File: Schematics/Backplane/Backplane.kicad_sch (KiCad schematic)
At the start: 21 parts, among them J1 Edge Connector (SLOT 1), J2 Edge Connector (SLOT 2), J3 Edge Connector (SLOT 3), J4 Edge Connector (SLOT 4), J5 Edge Connector (SLOT 5), J6 Conn_01x06_Socket

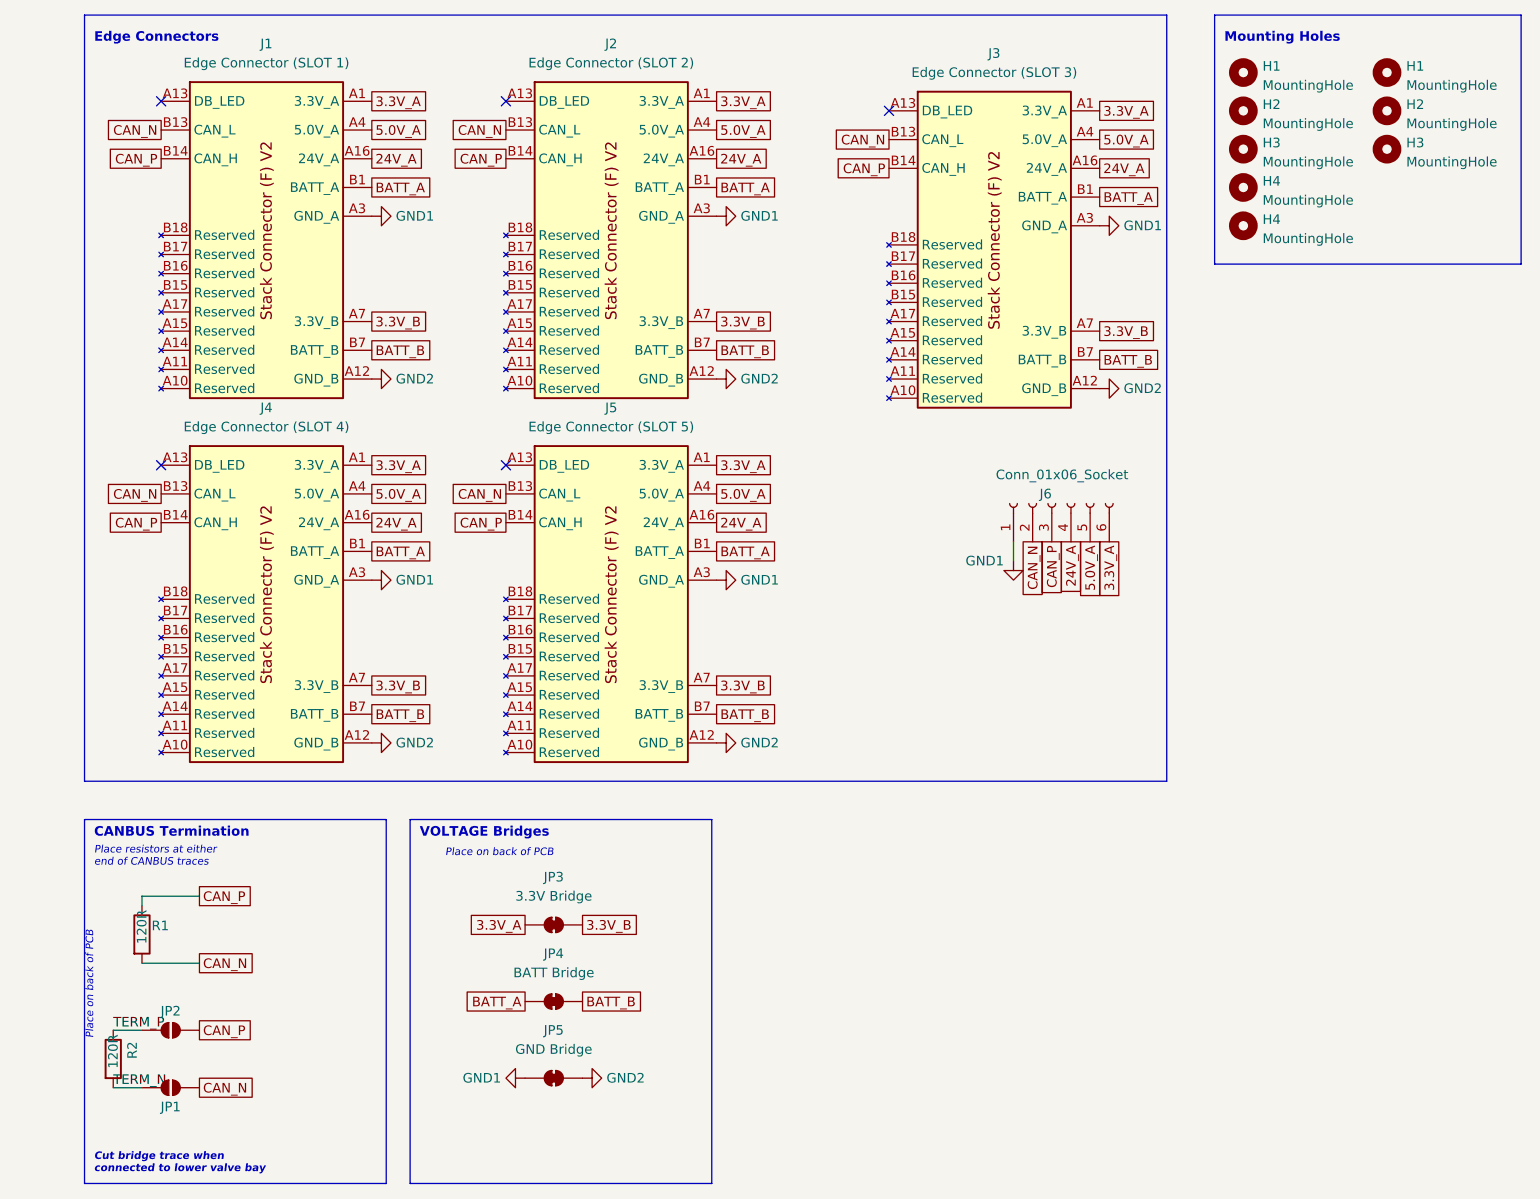
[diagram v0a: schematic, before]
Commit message: restored non hybrid backplane
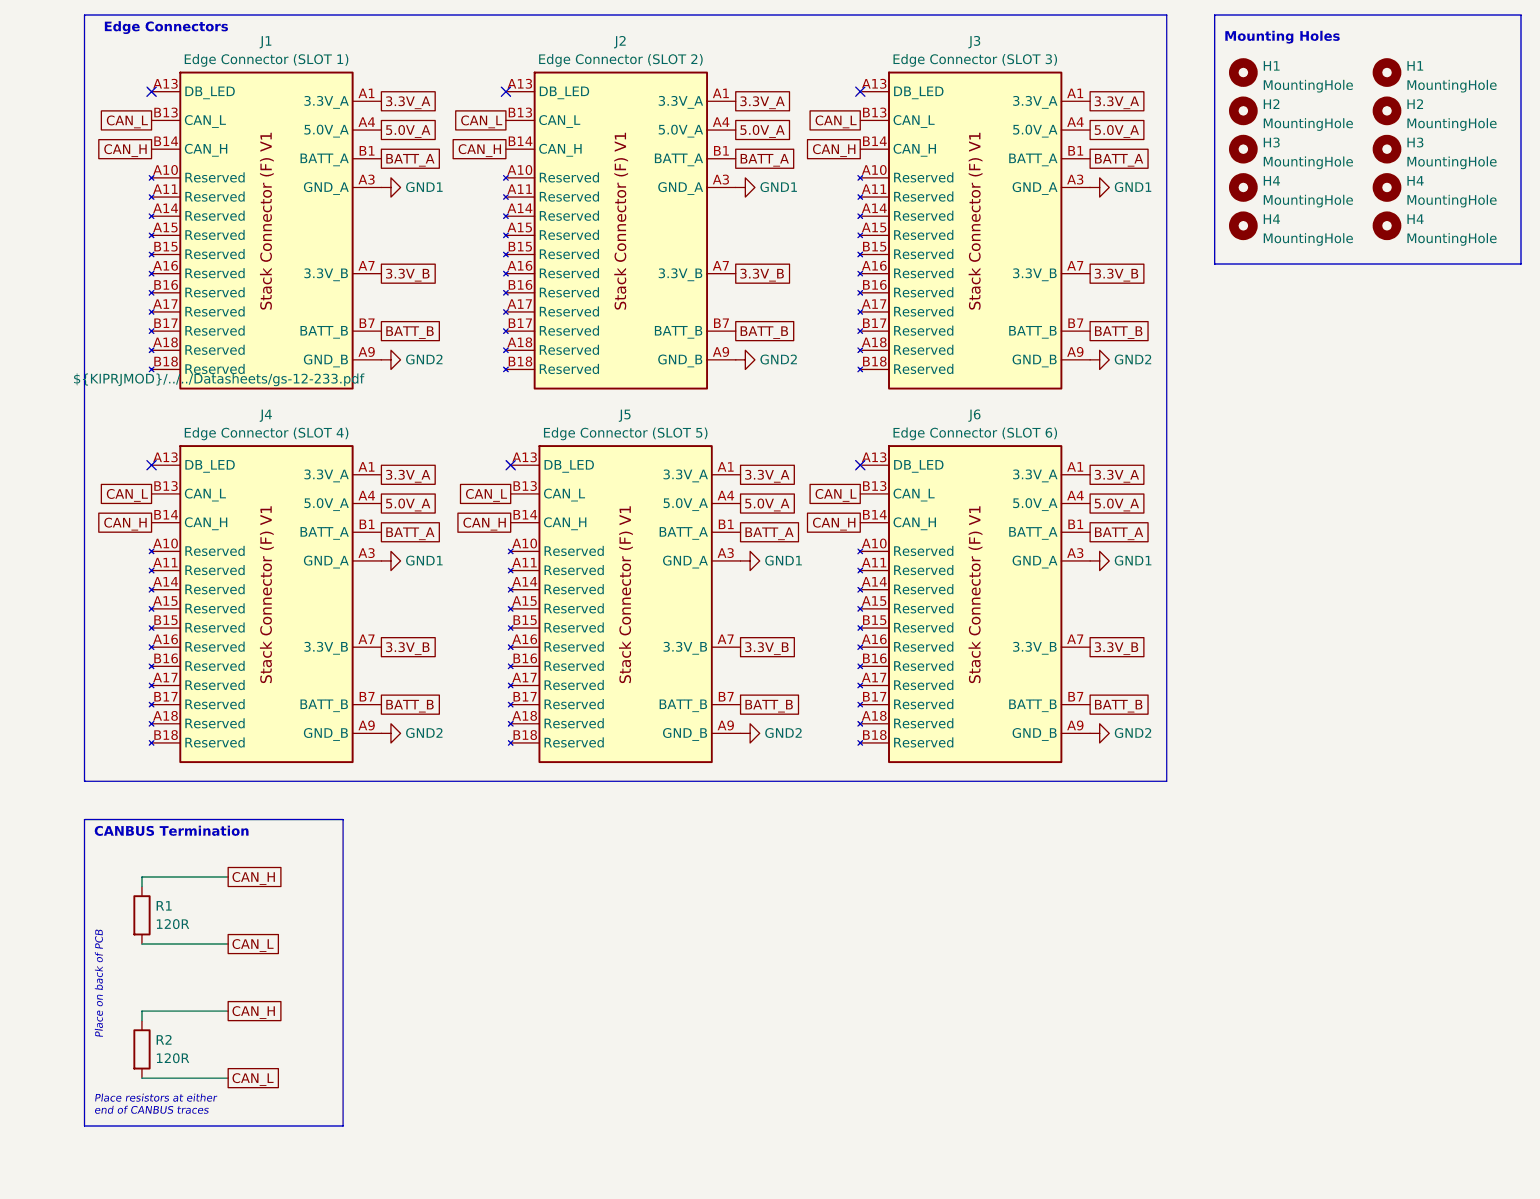
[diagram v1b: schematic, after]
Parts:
- removed J1: Edge Connector (SLOT 1), footprints:AMPHENOL_10018784-10210TLF, symbol EdgeConnnectorV2:Stack Female Edge Connector
- removed J2: Edge Connector (SLOT 2), footprints:AMPHENOL_10018784-10210TLF, symbol EdgeConnnectorV2:Stack Female Edge Connector
- removed J3: Edge Connector (SLOT 3), footprints:AMPHENOL_10018784-10210TLF, symbol EdgeConnnectorV2:Stack Female Edge Connector
- removed J4: Edge Connector (SLOT 4), footprints:AMPHENOL_10018784-10210TLF, symbol EdgeConnnectorV2:Stack Female Edge Connector
- removed J5: Edge Connector (SLOT 5), footprints:AMPHENOL_10018784-10210TLF, symbol EdgeConnnectorV2:Stack Female Edge Connector
- removed J6: Conn_01x06_Socket, footprints:CONN_SD-43045-001_06_MOL, symbol Connector:Conn_01x06_Socket
- removed JP1, JP2: SolderJumper_2_Open, Jumper:SolderJumper-2_P1.3mm_Open_RoundedPad1.0x1.5mm, symbol Jumper:SolderJumper_2_Open
- removed JP3: 3.3V Bridge, Jumper:SolderJumper-2_P1.3mm_Bridged2Bar_RoundedPad1.0x1.5mm, symbol Jumper:SolderJumper_2_Bridged
- removed JP4: BATT Bridge, Jumper:SolderJumper-2_P1.3mm_Bridged2Bar_RoundedPad1.0x1.5mm, symbol Jumper:SolderJumper_2_Bridged
- removed JP5: GND Bridge, Jumper:SolderJumper-2_P1.3mm_Bridged2Bar_RoundedPad1.0x1.5mm, symbol Jumper:SolderJumper_2_Bridged
- added H4 (x2): MountingHole, MountingHole:MountingHole_3.2mm_M3_ISO14580_Pad, symbol Mechanical:MountingHole
- added J1: Edge Connector (SLOT 1), footprints:AMPHENOL_10018784-10210TLF, symbol EdgeConnector:Stack Female Edge Connector
- added J2: Edge Connector (SLOT 2), footprints:AMPHENOL_10018784-10210TLF, symbol EdgeConnector:Stack Female Edge Connector
- added J3: Edge Connector (SLOT 3), footprints:AMPHENOL_10018784-10210TLF, symbol EdgeConnector:Stack Female Edge Connector
- added J4: Edge Connector (SLOT 4), footprints:AMPHENOL_10018784-10210TLF, symbol EdgeConnector:Stack Female Edge Connector
- added J5: Edge Connector (SLOT 5), footprints:AMPHENOL_10018784-10210TLF, symbol EdgeConnector:Stack Female Edge Connector
- added J6: Edge Connector (SLOT 6), footprints:AMPHENOL_10018784-10210TLF, symbol EdgeConnector:Stack Female Edge Connector
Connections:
- net TERM_N is gone; now on net CAN_L: R2.2
- net TERM_P is gone; now on net CAN_H: R2.1
- net 3.3V_A: now also J1.A1 (3.3V_A), J1.A2 (3.3V_A), J2.A1 (3.3V_A), J2.A2 (3.3V_A), J3.A1 (3.3V_A), J3.A2 (3.3V_A), J4.A1 (3.3V_A), J4.A2 (3.3V_A), J5.A1 (3.3V_A), J5.A2 (3.3V_A), J6.A1 (3.3V_A), J6.A2 (3.3V_A)
- net 3.3V_B: now also J1.A7 (3.3V_B), J1.A8 (3.3V_B), J2.A7 (3.3V_B), J2.A8 (3.3V_B), J3.A7 (3.3V_B), J3.A8 (3.3V_B), J4.A7 (3.3V_B), J4.A8 (3.3V_B), J5.A7 (3.3V_B), J5.A8 (3.3V_B), J6.A7 (3.3V_B), J6.A8 (3.3V_B)
- net 5.0V_A: now also J1.A4 (5.0V_A), J1.A5 (5.0V_A), J2.A4 (5.0V_A), J2.A5 (5.0V_A), J3.A4 (5.0V_A), J3.A5 (5.0V_A), J4.A4 (5.0V_A), J4.A5 (5.0V_A), J5.A4 (5.0V_A), J5.A5 (5.0V_A), J6.A4 (5.0V_A), J6.A5 (5.0V_A)
- net BATT_A: now also J1.B1 (BATT_A), J1.B2 (BATT_A), J1.B3 (BATT_A), J2.B1 (BATT_A), J2.B2 (BATT_A), J2.B3 (BATT_A), J3.B1 (BATT_A), J3.B2 (BATT_A), J3.B3 (BATT_A), J4.B1 (BATT_A), J4.B2 (BATT_A), J4.B3 (BATT_A), J5.B1 (BATT_A), J5.B2 (BATT_A), J5.B3 (BATT_A), J6.B1 (BATT_A), J6.B2 (BATT_A), J6.B3 (BATT_A)
- net BATT_B: now also J1.B7 (BATT_B), J1.B8 (BATT_B), J1.B9 (BATT_B), J2.B7 (BATT_B), J2.B8 (BATT_B), J2.B9 (BATT_B), J3.B7 (BATT_B), J3.B8 (BATT_B), J3.B9 (BATT_B), J4.B7 (BATT_B), J4.B8 (BATT_B), J4.B9 (BATT_B), J5.B7 (BATT_B), J5.B8 (BATT_B), J5.B9 (BATT_B), J6.B7 (BATT_B), J6.B8 (BATT_B), J6.B9 (BATT_B)
- net GND1: now also J1.A3 (GND_A), J1.A6 (GND_A), J1.B4 (GND_A), J1.B5 (GND_A), J1.B6 (GND_A), J2.A3 (GND_A), J2.A6 (GND_A), J2.B4 (GND_A), J2.B5 (GND_A), J2.B6 (GND_A), J3.A3 (GND_A), J3.A6 (GND_A), J3.B4 (GND_A), J3.B5 (GND_A), J3.B6 (GND_A), J4.A3 (GND_A), J4.A6 (GND_A), J4.B4 (GND_A), J4.B5 (GND_A), J4.B6 (GND_A), J5.A3 (GND_A), J5.A6 (GND_A), J5.B4 (GND_A), J5.B5 (GND_A), J5.B6 (GND_A), J6.A3 (GND_A), J6.A6 (GND_A), J6.B4 (GND_A), J6.B5 (GND_A), J6.B6 (GND_A)
- net GND2: now also J1.A12 (GND_B), J1.A9 (GND_B), J1.B10 (GND_B), J1.B11 (GND_B), J1.B12 (GND_B), J2.A12 (GND_B), J2.A9 (GND_B), J2.B10 (GND_B), J2.B11 (GND_B), J2.B12 (GND_B), J3.A12 (GND_B), J3.A9 (GND_B), J3.B10 (GND_B), J3.B11 (GND_B), J3.B12 (GND_B), J4.A12 (GND_B), J4.A9 (GND_B), J4.B10 (GND_B), J4.B11 (GND_B), J4.B12 (GND_B), J5.A12 (GND_B), J5.A9 (GND_B), J5.B10 (GND_B), J5.B11 (GND_B), J5.B12 (GND_B), J6.A12 (GND_B), J6.A9 (GND_B), J6.B10 (GND_B), J6.B11 (GND_B), J6.B12 (GND_B)
- net CAN_N renamed CAN_L
- net CAN_L: now also J1.B13 (CAN_L), J2.B13 (CAN_L), J3.B13 (CAN_L), J4.B13 (CAN_L), J5.B13 (CAN_L), J6.B13 (CAN_L)
- net CAN_P renamed CAN_H
- net CAN_H: now also J1.B14 (CAN_H), J2.B14 (CAN_H), J3.B14 (CAN_H), J4.B14 (CAN_H), J5.B14 (CAN_H), J6.B14 (CAN_H)
- no-connect marks 5 -> 6
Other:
- note removed: "Cut bridge trace when connected to lower valve bay"
- note removed: "VOLTAGE Bridges"
- moved on the sheet: R1

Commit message: init commit of hybrid backplane with new extension connector  - using bridges to merge POWER trace B with A for altimter  - add 120ohm termination bridge to allow CAN to work standlone
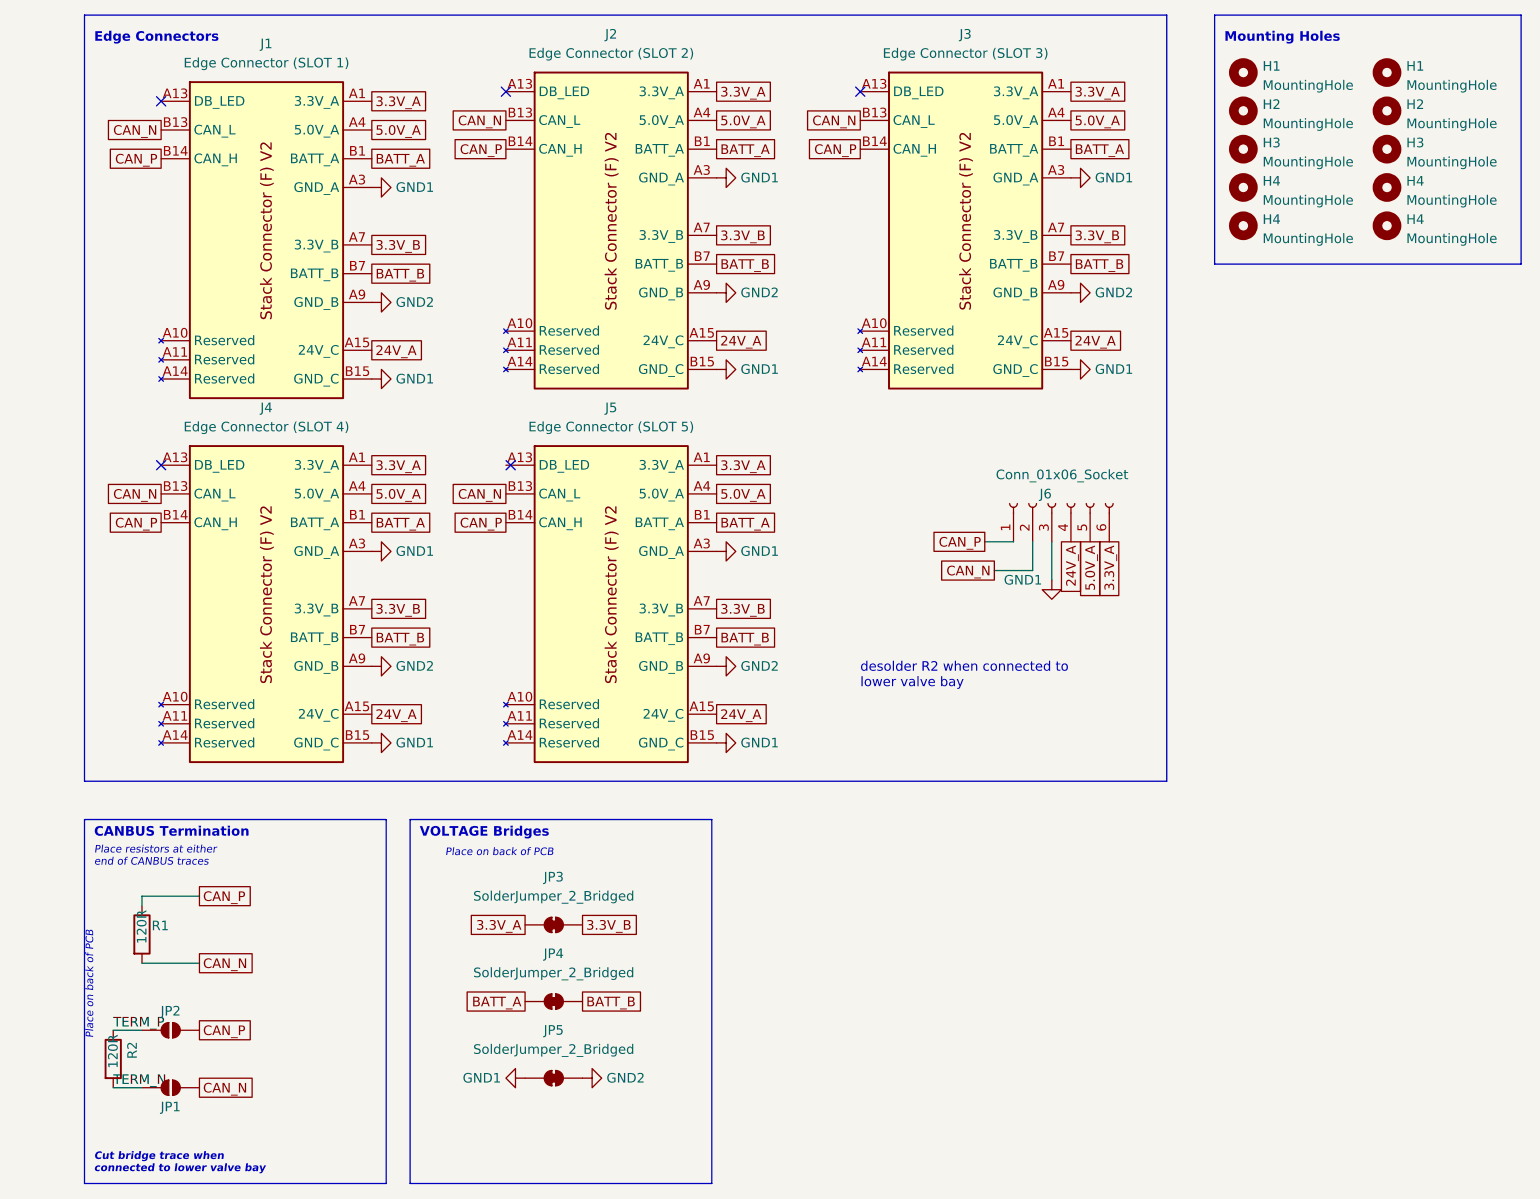
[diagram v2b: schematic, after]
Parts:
- removed J1: Edge Connector (SLOT 1), footprints:AMPHENOL_10018784-10210TLF, symbol EdgeConnector:Stack Female Edge Connector
- removed J2: Edge Connector (SLOT 2), footprints:AMPHENOL_10018784-10210TLF, symbol EdgeConnector:Stack Female Edge Connector
- removed J3: Edge Connector (SLOT 3), footprints:AMPHENOL_10018784-10210TLF, symbol EdgeConnector:Stack Female Edge Connector
- removed J4: Edge Connector (SLOT 4), footprints:AMPHENOL_10018784-10210TLF, symbol EdgeConnector:Stack Female Edge Connector
- removed J5: Edge Connector (SLOT 5), footprints:AMPHENOL_10018784-10210TLF, symbol EdgeConnector:Stack Female Edge Connector
- removed J6: Edge Connector (SLOT 6), footprints:AMPHENOL_10018784-10210TLF, symbol EdgeConnector:Stack Female Edge Connector
- added J1: Edge Connector (SLOT 1), footprints:AMPHENOL_10018784-10210TLF, symbol EdgeConnnectorV1.1:Stack Female Edge Connector
- added J2: Edge Connector (SLOT 2), footprints:AMPHENOL_10018784-10210TLF, symbol EdgeConnnectorV1.1:Stack Female Edge Connector
- added J3: Edge Connector (SLOT 3), footprints:AMPHENOL_10018784-10210TLF, symbol EdgeConnnectorV1.1:Stack Female Edge Connector
- added J4: Edge Connector (SLOT 4), footprints:AMPHENOL_10018784-10210TLF, symbol EdgeConnnectorV1.1:Stack Female Edge Connector
- added J5: Edge Connector (SLOT 5), footprints:AMPHENOL_10018784-10210TLF, symbol EdgeConnnectorV1.1:Stack Female Edge Connector
- added J6: Conn_01x06_Socket, footprints:CONN_SD-43045-001_06_MOL, symbol Connector:Conn_01x06_Socket
- added JP1, JP2: SolderJumper_2_Open, Jumper:SolderJumper-2_P1.3mm_Open_RoundedPad1.0x1.5mm, symbol Jumper:SolderJumper_2_Open
- added JP3, JP4, JP5: SolderJumper_2_Bridged, Jumper:SolderJumper-2_P1.3mm_Bridged2Bar_RoundedPad1.0x1.5mm, symbol Jumper:SolderJumper_2_Bridged
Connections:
- net 3.3V_A: now also J1.A1 (3.3V_A), J1.A2 (3.3V_A), J2.A1 (3.3V_A), J2.A2 (3.3V_A), J3.A1 (3.3V_A), J3.A2 (3.3V_A), J4.A1 (3.3V_A), J4.A2 (3.3V_A), J5.A1 (3.3V_A), J5.A2 (3.3V_A), J6.6 (Pin_6), JP3.1 (A)
- net 3.3V_B: now also J1.A7 (3.3V_B), J1.A8 (3.3V_B), J2.A7 (3.3V_B), J2.A8 (3.3V_B), J3.A7 (3.3V_B), J3.A8 (3.3V_B), J4.A7 (3.3V_B), J4.A8 (3.3V_B), J5.A7 (3.3V_B), J5.A8 (3.3V_B), JP3.2 (B)
- net 5.0V_A: now also J1.A4 (5.0V_A), J1.A5 (5.0V_A), J2.A4 (5.0V_A), J2.A5 (5.0V_A), J3.A4 (5.0V_A), J3.A5 (5.0V_A), J4.A4 (5.0V_A), J4.A5 (5.0V_A), J5.A4 (5.0V_A), J5.A5 (5.0V_A), J6.5 (Pin_5)
- net BATT_A: now also J1.B1 (BATT_A), J1.B2 (BATT_A), J1.B3 (BATT_A), J2.B1 (BATT_A), J2.B2 (BATT_A), J2.B3 (BATT_A), J3.B1 (BATT_A), J3.B2 (BATT_A), J3.B3 (BATT_A), J4.B1 (BATT_A), J4.B2 (BATT_A), J4.B3 (BATT_A), J5.B1 (BATT_A), J5.B2 (BATT_A), J5.B3 (BATT_A), JP4.1 (A)
- net BATT_B: now also J1.B7 (BATT_B), J1.B8 (BATT_B), J1.B9 (BATT_B), J2.B7 (BATT_B), J2.B8 (BATT_B), J2.B9 (BATT_B), J3.B7 (BATT_B), J3.B8 (BATT_B), J3.B9 (BATT_B), J4.B7 (BATT_B), J4.B8 (BATT_B), J4.B9 (BATT_B), J5.B7 (BATT_B), J5.B8 (BATT_B), J5.B9 (BATT_B), JP4.2 (B)
- net GND1: now also J1.A3 (GND_A), J1.A6 (GND_A), J1.B15 (GND_C), J1.B16 (GND_C), J1.B17 (GND_C), J1.B18 (GND_C), J1.B4 (GND_A), J1.B5 (GND_A), J1.B6 (GND_A), J2.A3 (GND_A), J2.A6 (GND_A), J2.B15 (GND_C), J2.B16 (GND_C), J2.B17 (GND_C), J2.B18 (GND_C), J2.B4 (GND_A), J2.B5 (GND_A), J2.B6 (GND_A), J3.A3 (GND_A), J3.A6 (GND_A), J3.B15 (GND_C), J3.B16 (GND_C), J3.B17 (GND_C), J3.B18 (GND_C), J3.B4 (GND_A), J3.B5 (GND_A), J3.B6 (GND_A), J4.A3 (GND_A), J4.A6 (GND_A), J4.B15 (GND_C), J4.B16 (GND_C), J4.B17 (GND_C), J4.B18 (GND_C), J4.B4 (GND_A), J4.B5 (GND_A), J4.B6 (GND_A), J5.A3 (GND_A), J5.A6 (GND_A), J5.B15 (GND_C), J5.B16 (GND_C), J5.B17 (GND_C), J5.B18 (GND_C), J5.B4 (GND_A), J5.B5 (GND_A), J5.B6 (GND_A), J6.3 (Pin_3), JP5.1 (A)
- net GND2: now also J1.A12 (GND_B), J1.A9 (GND_B), J1.B10 (GND_B), J1.B11 (GND_B), J1.B12 (GND_B), J2.A12 (GND_B), J2.A9 (GND_B), J2.B10 (GND_B), J2.B11 (GND_B), J2.B12 (GND_B), J3.A12 (GND_B), J3.A9 (GND_B), J3.B10 (GND_B), J3.B11 (GND_B), J3.B12 (GND_B), J4.A12 (GND_B), J4.A9 (GND_B), J4.B10 (GND_B), J4.B11 (GND_B), J4.B12 (GND_B), J5.A12 (GND_B), J5.A9 (GND_B), J5.B10 (GND_B), J5.B11 (GND_B), J5.B12 (GND_B), JP5.2 (B)
- net CAN_H renamed CAN_P
- net CAN_P: now also J1.B14 (CAN_H), J2.B14 (CAN_H), J3.B14 (CAN_H), J4.B14 (CAN_H), J5.B14 (CAN_H), J6.1 (Pin_1), JP2.1 (A); no longer R2.1
- net CAN_L renamed CAN_N
- net CAN_N: now also J1.B13 (CAN_L), J2.B13 (CAN_L), J3.B13 (CAN_L), J4.B13 (CAN_L), J5.B13 (CAN_L), J6.2 (Pin_2), JP1.1 (A); no longer R2.2
- new net 24V_A: J1.A15 (24V_C), J1.A16 (24V_C), J1.A17 (24V_C), J1.A18 (24V_C), J2.A15 (24V_C), J2.A16 (24V_C), J2.A17 (24V_C), J2.A18 (24V_C), J3.A15 (24V_C), J3.A16 (24V_C), J3.A17 (24V_C), J3.A18 (24V_C), J4.A15 (24V_C), J4.A16 (24V_C), J4.A17 (24V_C), J4.A18 (24V_C), J5.A15 (24V_C), J5.A16 (24V_C), J5.A17 (24V_C), J5.A18 (24V_C), J6.4 (Pin_4)
- new net TERM_N: JP1.2 (B), R2.2
- new net TERM_P: JP2.2 (B), R2.1
- no-connect marks 6 -> 5
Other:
- note added: "Cut bridge trace when connected to lower valve bay"
- note added: "VOLTAGE Bridges"
- note added: "desolder R2 when connected to lower valve bay"
- moved on the sheet: R1
